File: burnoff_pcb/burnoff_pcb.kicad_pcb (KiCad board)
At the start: 2 copper layers, 61 x 69.8 mm, 41 parts, among them J1 Conn_01x06_Male, Q1 Q_NMOS_SGD, Q2 Q_PMOS_GDS, Q3 Q_NMOS_SGD, Q4 Q_PMOS_GDS, Q5 Q_NMOS_SGD, Q6 Q_PMOS_GDS, U1 NA555P, U2 LP2950-5.0_TO92, U3 LM2903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

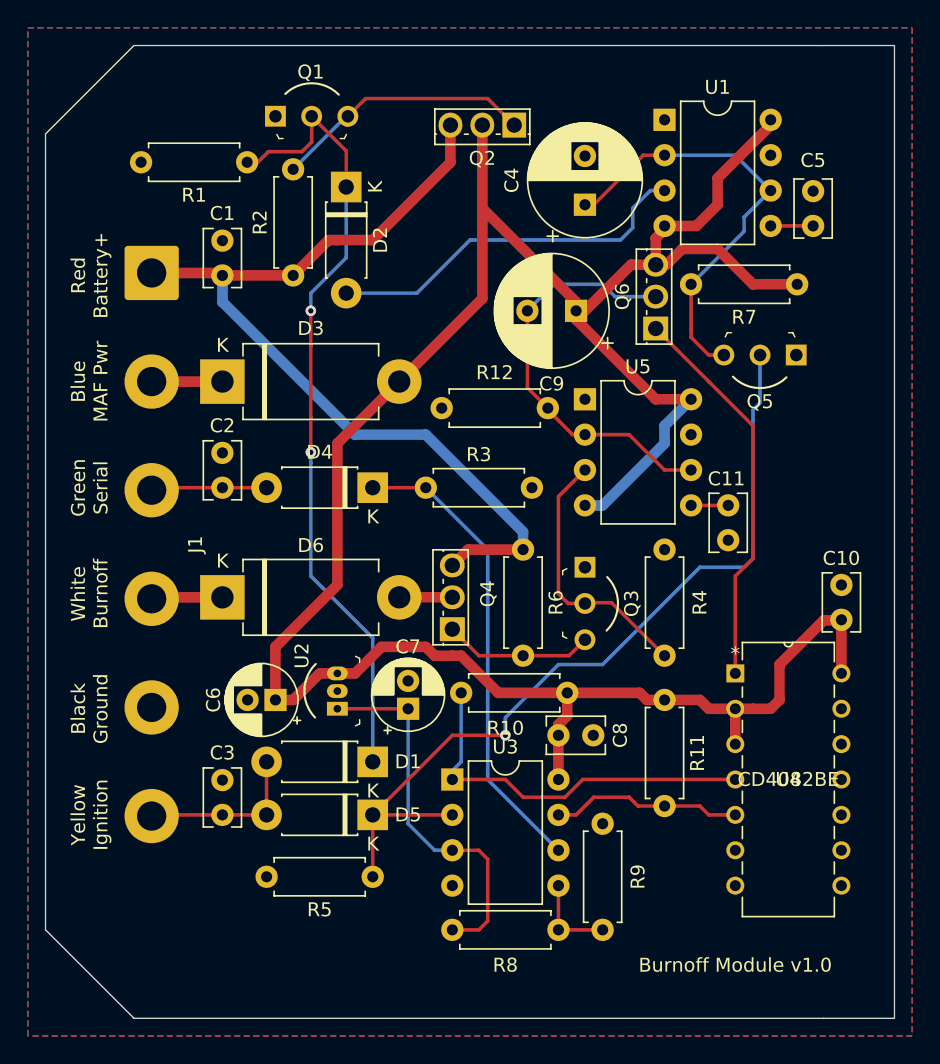
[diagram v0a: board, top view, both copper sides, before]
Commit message: Update to version v1.1 of the schematic/pcb layout.
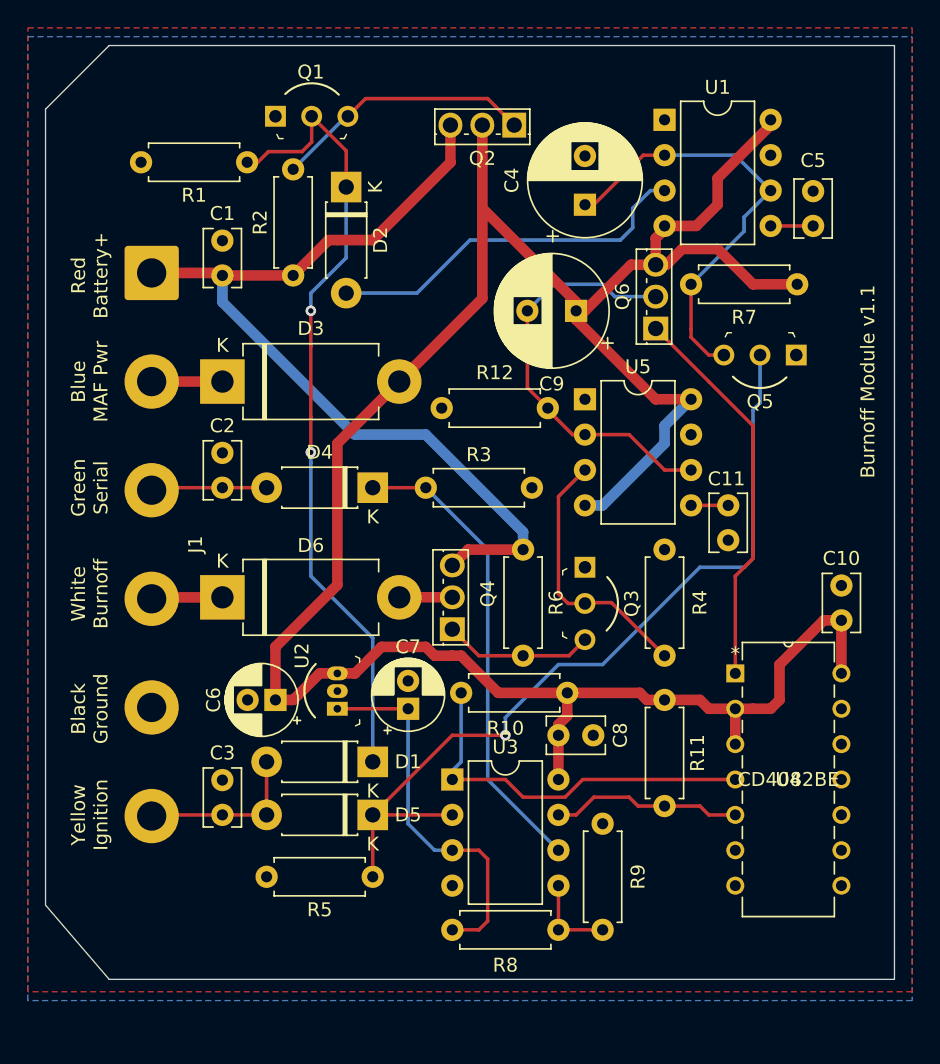
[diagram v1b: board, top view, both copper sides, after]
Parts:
- moved C10 2.54 mm to (108.0, 128.9), turned to 90 degrees
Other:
- board size 61 x 69.8 mm -> 61 x 67.1 mm
- board text added: "Burnoff Module v1.1"
- board text removed: "Burnoff Module v1.0"
